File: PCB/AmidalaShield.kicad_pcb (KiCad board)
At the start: 4 copper layers, 100 x 75 mm, 37 parts, among them J1 Screw_Terminal_01x02, J3 Micro_SD_Card

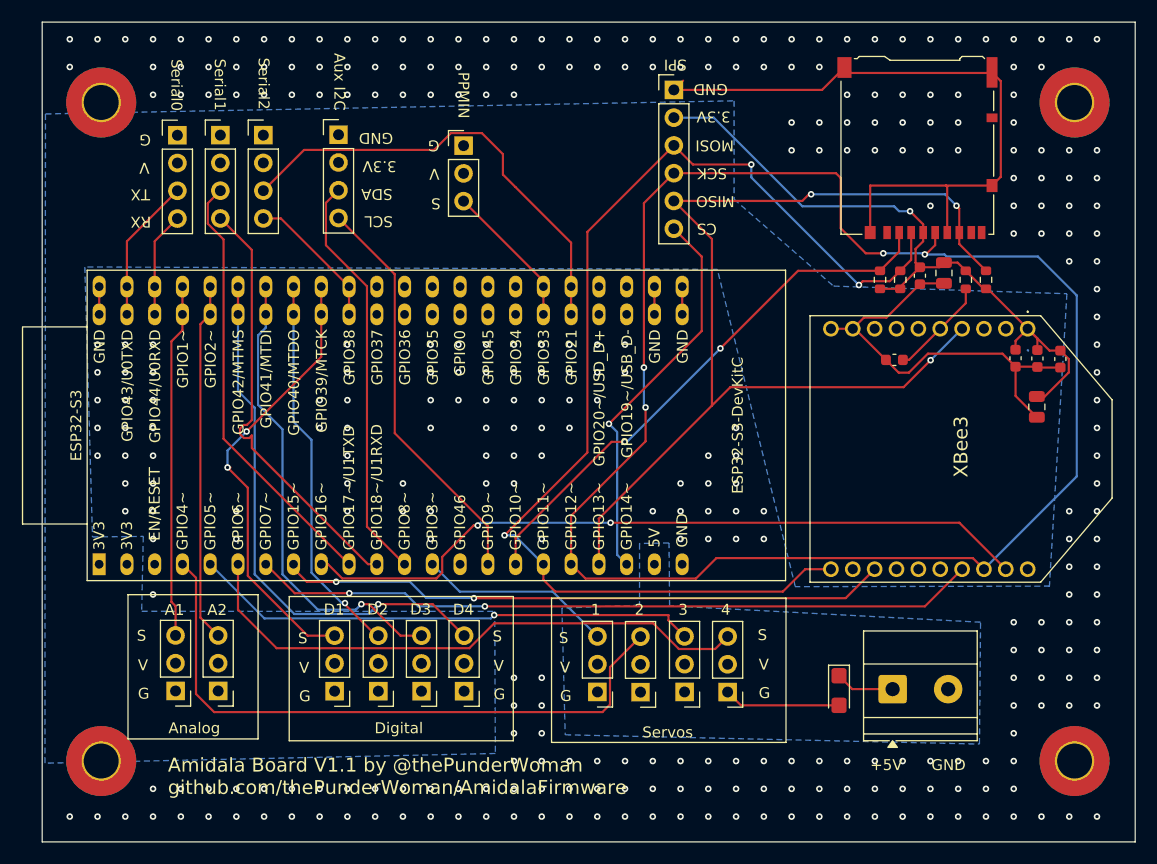
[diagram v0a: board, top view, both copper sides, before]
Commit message: Board V1.2 minor polish
This adds some graphics and ensures the board definitely comes in at just under the 100mm width mark for price benefits.
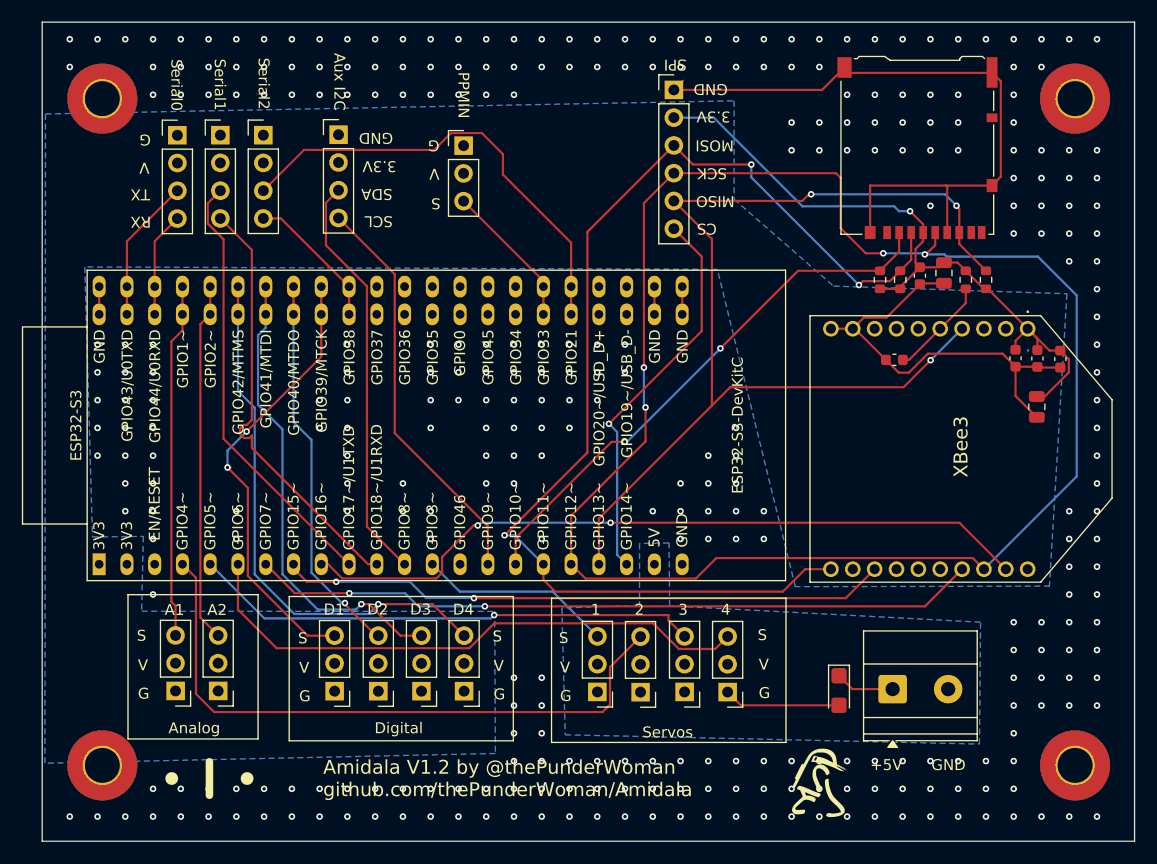
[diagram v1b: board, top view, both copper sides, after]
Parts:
- added G***: LOGO, Amidala:R2Builders, F.Cu at (137.6, 105.6)
- added G***: LOGO, Amidala:amidala-logo, F.Cu at (81.8, 105.2)
- moved REF** 0.41 mm to (72.0, 104.0)
- moved REF** 0.40 mm to (161.0, 104.0)
- moved REF** 0.36 mm to (72.0, 43.0)
- moved REF** 0.35 mm to (161.0, 43.0)
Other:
- board size 100 x 75 mm -> 99.9 x 74.9 mm
- board text added: "Amidala V1.2 by @thePunderWoman github.com/thePunderWoman/Amidala"
- board text removed: "Amidala Board V1.1 by @thePunderWoman github.com/thePunderWoman/AmidalaFirmware"

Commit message: refactor: Update PCB with power jumper
This adds a jumper to connect the digital and analog pins to either 3.3v or 5v depending on the jumper position.
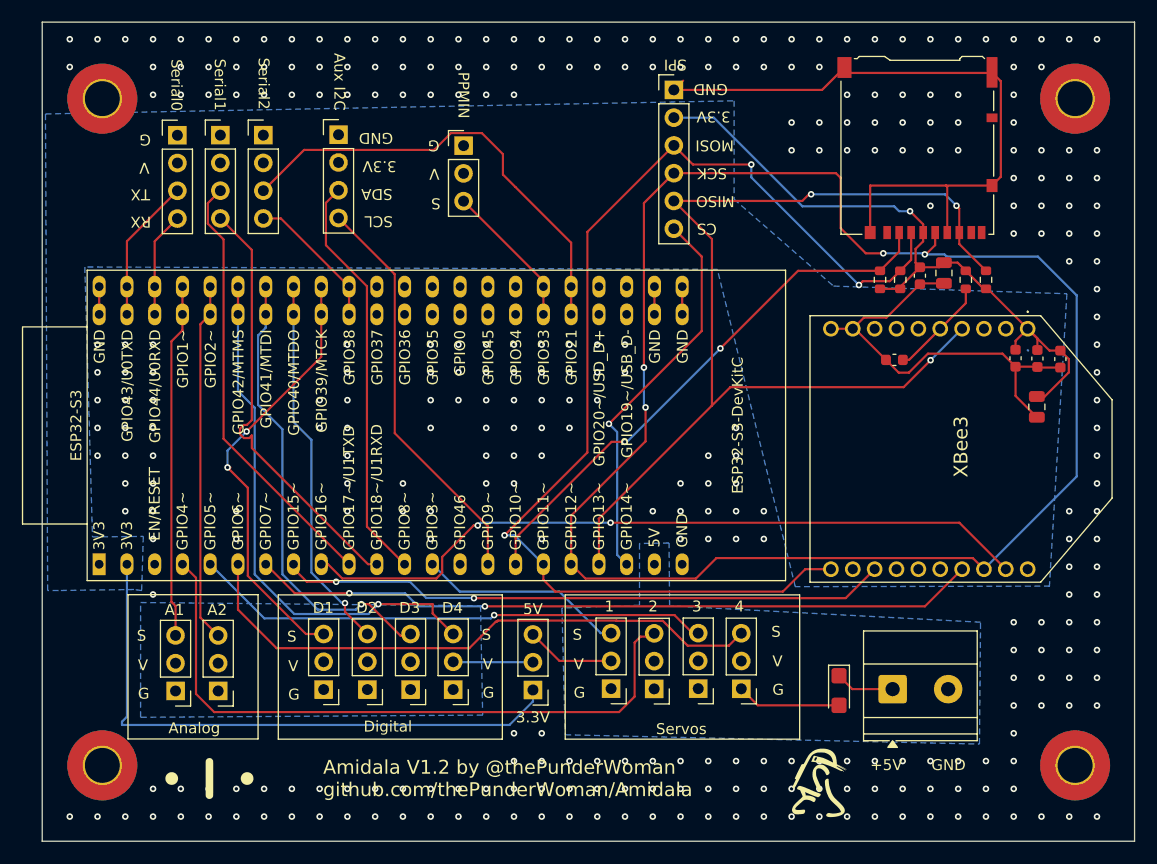
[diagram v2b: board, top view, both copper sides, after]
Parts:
- added JP1: Jumper_3_Open, Connector_PinHeader_2.54mm:PinHeader_1x03_P2.54mm_Vertical, F.Cu at (111.4, 97.1)
- moved J_Servo4 1.29 mm to (130.5, 97.0)
- moved J_Servo1 1.29 mm to (118.5, 97.0)
- moved J_Servo2 1.29 mm to (122.5, 97.0)
- moved J_Servo3 1.29 mm to (126.5, 97.0)
- moved J_Digital1 1.01 mm to (92.2, 97.1)
- moved J_Digital2 1.01 mm to (96.2, 97.1)
- moved J_Digital3 1.01 mm to (100.2, 97.1)
- moved J_Digital4 1.01 mm to (104.1, 97.1)
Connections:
- J_Analog1 pad 2: +3.3V -> VCC_DIG
- J_Analog2 pad 2: +3.3V -> VCC_DIG
- J_Digital1 pad 2: +3.3V -> VCC_DIG
- J_Digital2 pad 2: +3.3V -> VCC_DIG
- J_Digital3 pad 2: +3.3V -> VCC_DIG
- J_Digital4 pad 2: +3.3V -> VCC_DIG
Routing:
- net +3.3V: track 63.5 -> 117.9 mm
- net +5V: track 5.41 -> 13.6 mm
- net VCC_DIG: track 0.00 -> 7.32 mm
- net /Servos/GPIO4: track 58.6 -> 60.9 mm
- net /Servos/GPIO6: track 52.8 -> 54.1 mm
- net /Servos/GPIO3: track 17.8 -> 19.0 mm
- net GND: track 120.0 -> 118.9 mm, vias 333 -> 329
- net /Pins/GPIO39: track 41.3 -> 40.2 mm
- net /Pins/GPIO41: track 43.0 -> 42.1 mm
- net /Servos/GPIO5: track 46.7 -> 47.5 mm
- net /Pins/GPIO40: track 35.4 -> 34.8 mm
- net /Pins/GPIO42: track 49.2 -> 48.6 mm
- added copper zone on B.Cu, net VCC_DIG
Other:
- board text added: "5V"
